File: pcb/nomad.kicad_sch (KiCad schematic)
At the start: 35 parts, among them J1 USB_C_Receptacle_USB2.0_16P, SW1 UP, SW2 DOWN, SW3 RIGHT, SW4 LEFT, SW5 SEL, SW6 SW_Push, SW7 SW_Push, U1 ESP32-S3-WROOM-1, U2 PCF8574T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

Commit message: Updating PCB
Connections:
- net SCL: now also U1.17 (IO9)
- net SDA: now also U1.12 (IO8)
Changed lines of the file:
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@@
+		)
+	)
+	(global_label "FLASHLIGHT"
+		(shape input)
+		(at 195.58 87.63 0)
+		(fields_autoplaced yes)
+		(effects
+			(font
+				(size 1.27 1.27)
+			)
+			(justify left)
+		)
+		(property "Intersheetrefs" "${INTERSHEET_REFS}"
+			(at 209.5115 87.63 0)
+			(hide yes)
+			(show_name no)
+			(do_not_autoplace no)
+			(effects
+				(font
+					(size 1.27 1.27)
+				)
+				(justify left)
+			)
 		)
 	)
@@
 		)
 	)
+	(global_label "SCL"
+		(shape input)
+		(at 236.22 59.69 180)
+		(fields_autoplaced yes)
+		(effects
+			(font
+				(size 1.27 1.27)
+			)
+			(justify right)
+		)
+		(property "Intersheetrefs" "${INTERSHEET_REFS}"
+			(at 229.7272 59.69 0)
+			(hide yes)
+			(show_name no)
+			(do_not_autoplace no)
+			(effects
+				(font
+					(size 1.27 1.27)
+				)
+				(justify right)
+			)
+		)
+	)
 	(global_label "BUTTON_INT"
 		(shape input)
@@
 			)
 		)
+	)
+	(global_label "SDA"
+		(shape input)
+		(at 236.22 57.15 180)
+		(fields_autoplaced yes)
+		(effects
+			(font
+				(size 1.27 1.27)
+			)
+			(justify right)
+		)
+		(property "Intersheetrefs" "${INTERSHEET_REFS}"
+			(at 229.6667 57.15 0)
+			(hide yes)
+			(show_name no)
+			(do_not_autoplace no)
+			(effects
+				(font
+					(size 1.27 1.27)
+				)
+				(justify right)
+			)
+		)

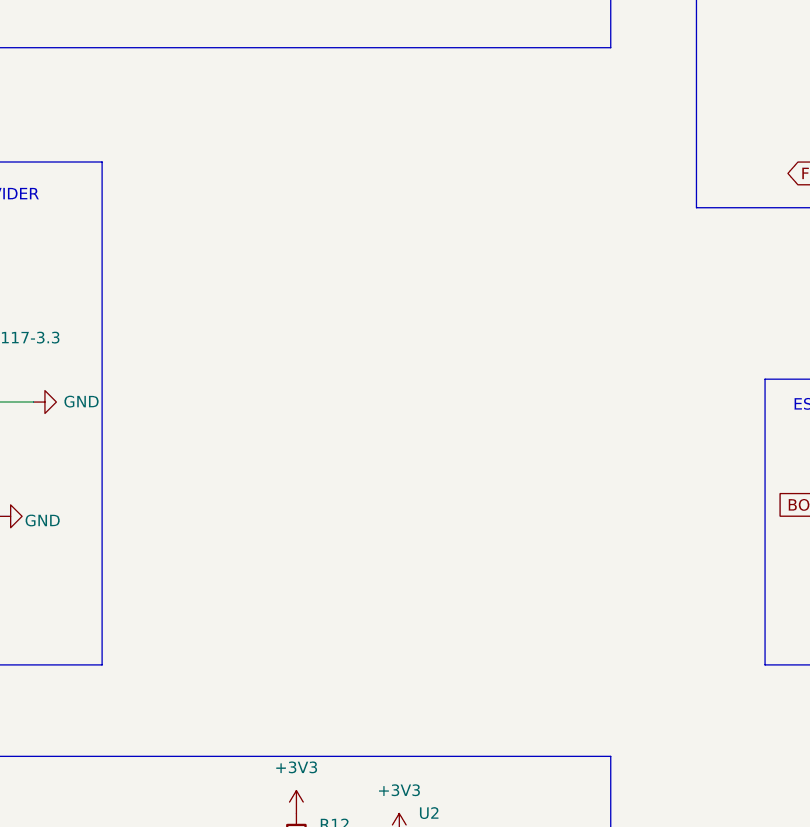
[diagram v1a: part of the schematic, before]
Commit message: Updating footprints & shematics + replacing components on PCB
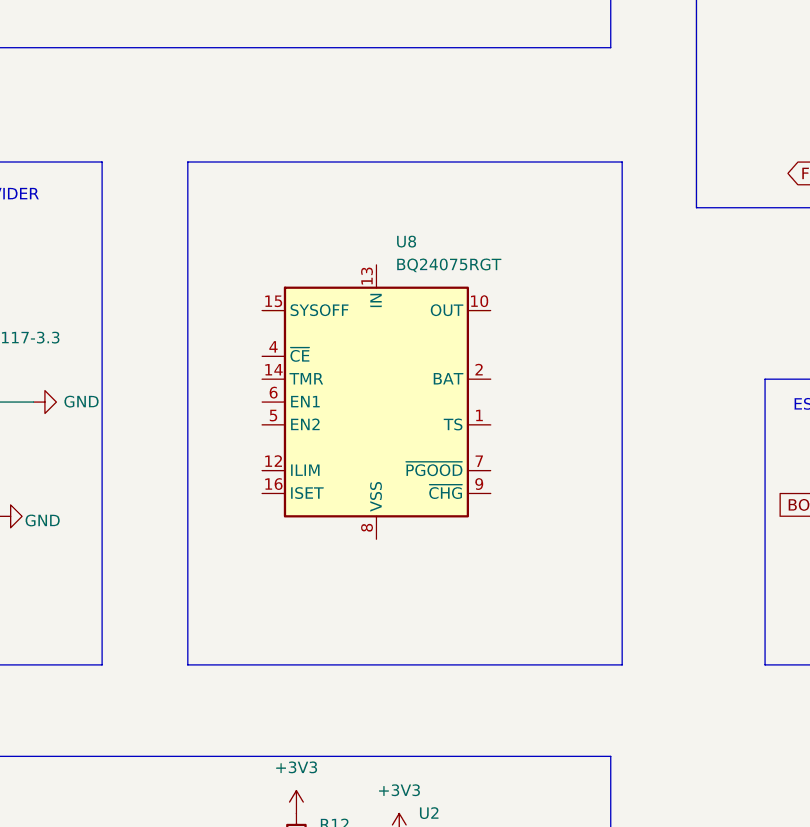
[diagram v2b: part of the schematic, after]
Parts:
- added U8: BQ24075RGT, Package_DFN_QFN:VQFN-16-1EP_3x3mm_P0.5mm_EP1.6x1.6mm, symbol Battery_Management:BQ24075RGT
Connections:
- new net: U8.10 (OUT), U8.11 (OUT)
- new net: U8.17 (VSS), U8.8 (VSS)
- new net: U8.2 (BAT), U8.3 (BAT)
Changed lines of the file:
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@@
 	)
 	(rectangle
+		(start 128.905 86.36)
+		(end 177.165 142.24)
+		(stroke
+			(width 0)
+			(type default)
+		)
+		(fill
+			(type none)
+		)
+	)
+	(rectangle
 		(start 193.04 110.49)
 		(end 260.35 142.24)
@@
 					(unit 1)
 				)
+			)
+		)
+	)
+	(symbol
+		(lib_id "Battery_Management:BQ24075RGT")
+		(at 149.86 113.03 0)
+		(unit 1)
+		(body_style 1)
+		(exclude_from_sim no)
+		(in_bom yes)
+		(on_board yes)
+		(in_pos_files yes)
+		(dnp no)
+		(fields_autoplaced yes)
+		(property "Reference" "U8"
+			(at 152.0033 95.25 0)
+			(show_name no)
+			(do_not_autoplace no)
+			(effects
+				(font
+					(size 1.27 1.27)
+				)
+				(justify left)
+			)
+		)
+		(property "Value" "BQ24075RGT"
+			(at 152.0033 97.79 0)
+			(show_name no)
+			(do_not_autoplace no)
+			(effects
+				(font
+					(size 1.27 1.27)
+				)
+				(justify left)
+			)
+		)
+		(property "Footprint" "Package_DFN_QFN:VQFN-16-1EP_3x3mm_P0.5mm_EP1.6x1.6mm"
+			(at 157.48 127 0)
+			(hide yes)
+			(show_name no)
+			(do_not_autoplace no)
+			(effects
+				(font
+					(size 1.27 1.27)
+				)
+				(justify left)
+			)
+		)
+		(property "Datasheet" "http://www.ti.com/lit/ds/symlink/bq24075.pdf"
+			(at 157.48 107.95 0)
+			(hide yes)
+			(show_name no)
+			(do_not_autoplace no)
+			(effects
+				(font
+					(size 1.27 1.27)
+				)
+			)
+		)
+		(property "Description" "USB-Friendly Li-Ion Battery Charger and Power-Path Management, VQFN-16"
+			(at 149.86 113.03 0)
+			(hide yes)
+			(show_name no)
+			(do_not_autoplace no)
+			(effects
+				(font
+					(size 1.27 1.27)
+				)
+			)
+		)
+		(pin "14"
+		)
+		(pin "15"
+		)
+		(pin "6"
+		)
+		(pin "5"
+		)
+		(pin "1"
+		)
+		(pin "2"
+		)
+		(pin "3"
+		)
+		(pin "9"
+		)
+		(pin "10"
+		)
+		(pin "4"
+		)
+		(pin "8"
+		)
+		(pin "11"
+		)
+		(pin "12"
+		)
+		(pin "16"
+		)
+		(pin "13"
+		)
+		(pin "17"
+		)
+		(pin "7"
+		)
+		(instances
+			(project "nomad"
+				(path "/76473bbd-feb6-4b7c-8160-a4d55fa11a55"
+					(reference "U8")
+					(unit 1)
+				)

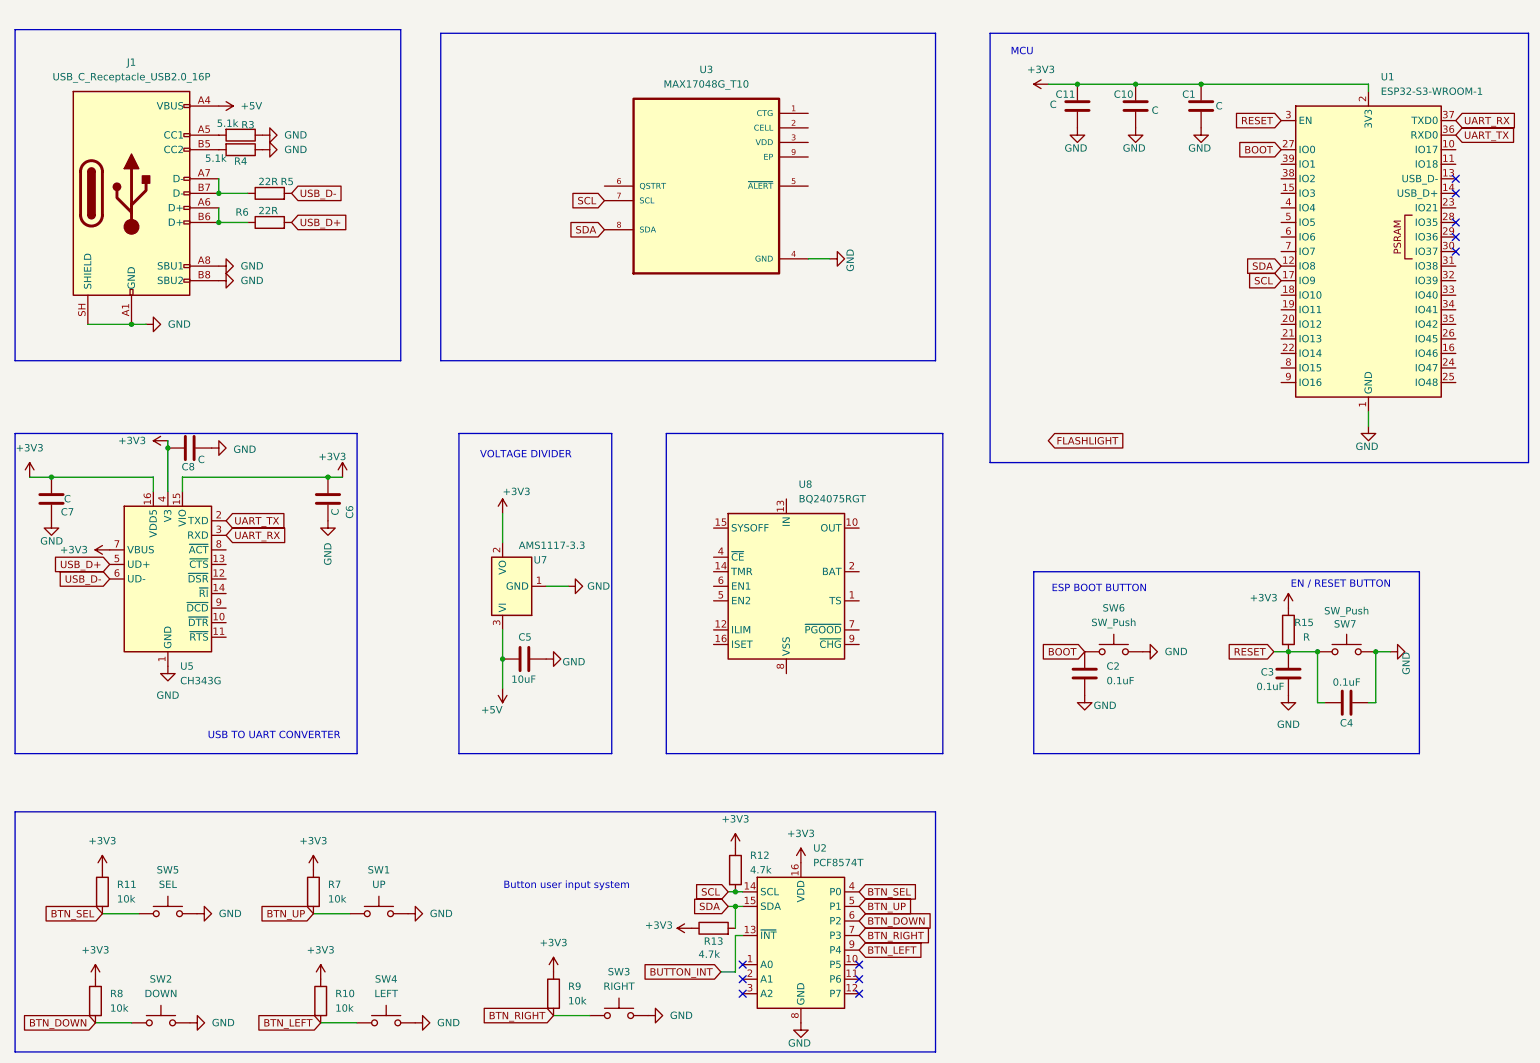
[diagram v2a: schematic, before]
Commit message: Wiring MAX17048 battery percentage module
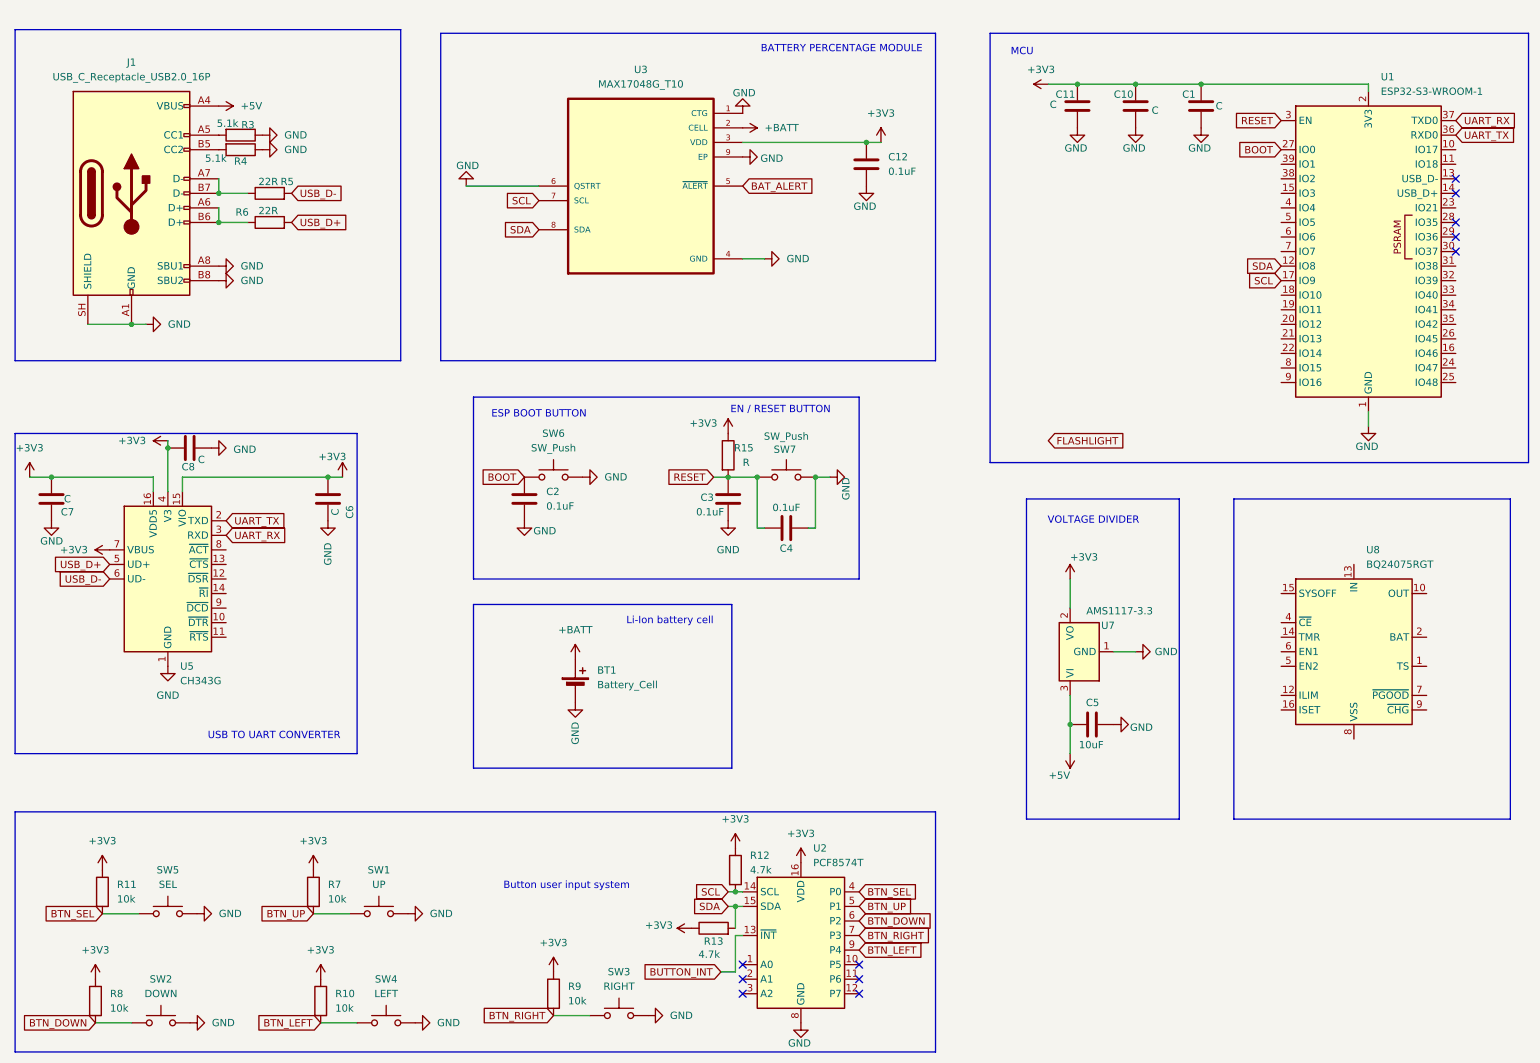
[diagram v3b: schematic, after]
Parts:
- added BT1: Battery_Cell, symbol Device:Battery_Cell
- added C12: 0.1uF, symbol Device:C
- SW1, SW2, SW3, SW4, SW5: footprint Button_Switch_THT:SW_PUSH_6mm -> Button_Switch_SMD:SW_Push_1P1T_NO_E-Switch_TL3301NxxxxxG
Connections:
- net +3V3: now also U3.3 (VDD), C12.1
- net GND: now also U3.1 (CTG), U3.6 (QSTRT), U3.9 (EP), BT1.2 (-), C12.2
- net +BATT: now reaches U3.2 (CELL)
- net +BATT: now also BT1.1 (+)
- net BAT_ALERT: now reaches U3.5 (~{ALERT})
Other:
- note added: "BATTERY PERCENTAGE MODULE"
- note added: "Li-Ion battery cell"
- moved on the sheet: C2, C3, C4, C5, R15, SW6, SW7, U3, U7, U8

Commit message: Updating PCB
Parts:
- removed C6, C7, C8: C, Capacitor_SMD:C_0805_2012Metric, symbol Device:C
- removed U5: CH343G, Package_SO:SOIC-16_3.9x9.9mm_P1.27mm, symbol Interface_USB:CH343G
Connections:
- net USB_D+: now also U1.14 (USB_D+)
- net USB_D-: now also U1.13 (USB_D-)
- net UART_RX: no longer names the net of U1.37 (TXD0)
- no-connect marks 11 -> 10
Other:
- note added: "BATTERY MANAGEMENT"
- note added: "BATTERY SECURITY"
- note added: "USB-C FEMALE PORT FOR CHARGE AND DATA"
- note removed: "USB TO UART CONVERTER"
- moved on the sheet: BT1, C2, C3, C4, R15, SW6, SW7

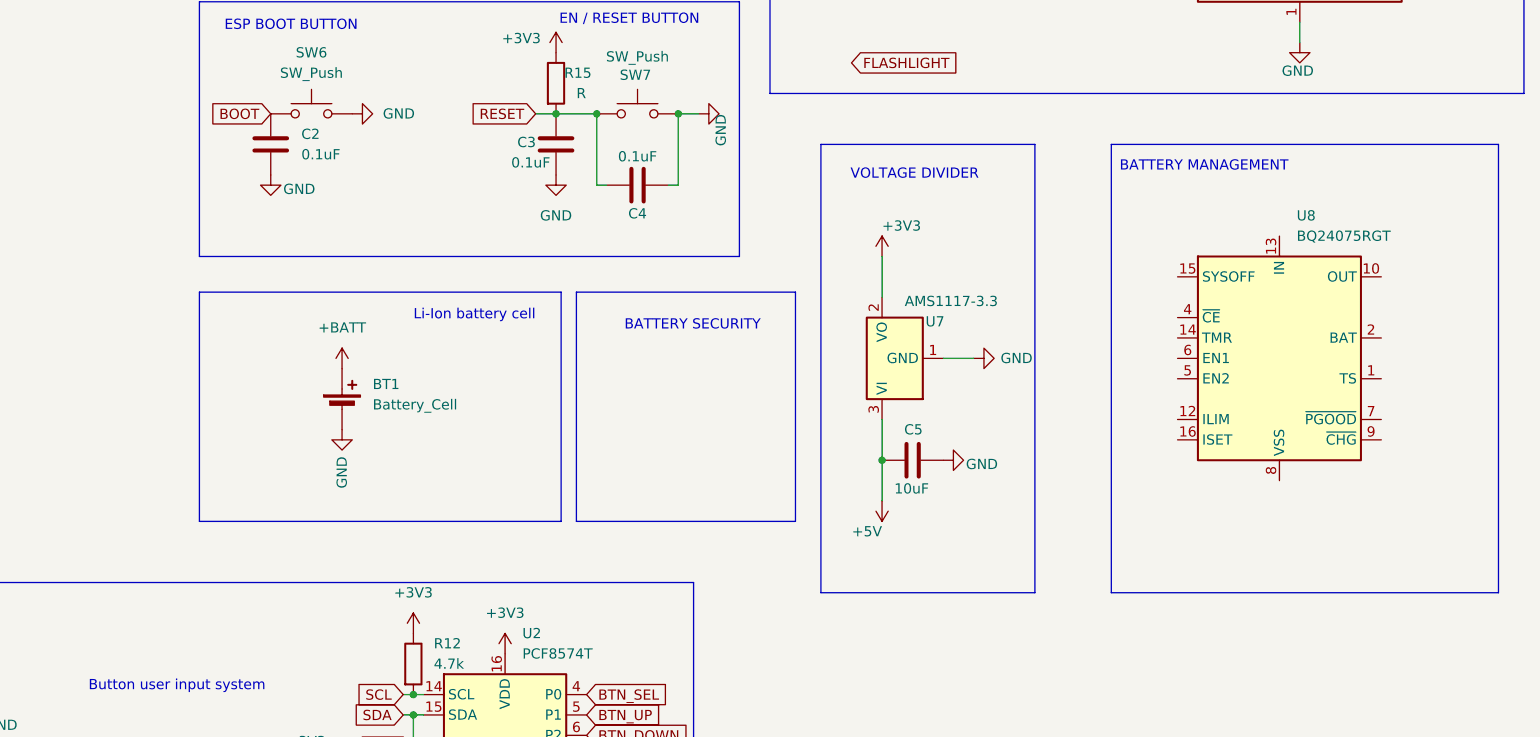
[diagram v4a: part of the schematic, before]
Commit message: Adding battery management system with  MCP73831 chip.
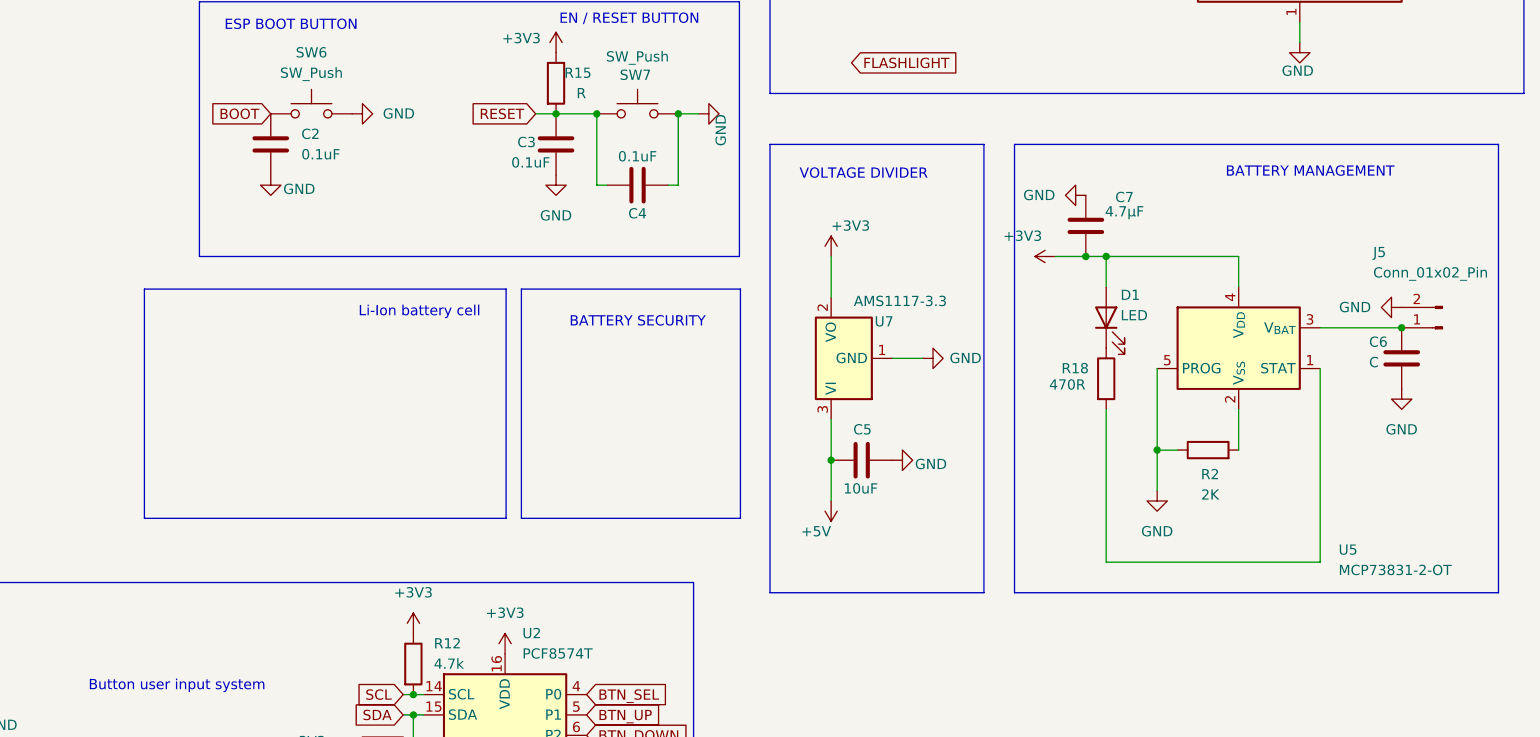
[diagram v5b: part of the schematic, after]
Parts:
- removed BT1: Battery_Cell, symbol Device:Battery_Cell
- removed U8: BQ24075RGT, Package_DFN_QFN:VQFN-16-1EP_3x3mm_P0.5mm_EP1.6x1.6mm, symbol Battery_Management:BQ24075RGT
- added C6: C, Capacitor_SMD:C_0805_2012Metric, symbol Device:C
- added C7: 4.7µF, Capacitor_SMD:C_0805_2012Metric, symbol Device:C
- added D1: LED, symbol Device:LED
- added J5: Conn_01x02_Pin, JST_PH_S2B-PH-K_1x02_P2.00mm_Horizontal, symbol Connector:Conn_01x02_Pin
- added R18: 470R, symbol Device:R
- added R2: 2K, Resistor_SMD:R_0805_2012Metric, symbol Device:R
- added U5: MCP73831-2-OT, Package_TO_SOT_SMD:SOT-23-5, symbol Battery_Management:MCP73831-2-OT
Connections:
- net +3V3: now also C7.1, D1.2 (A), U5.4 (V_{DD})
- net GND: now also C6.2, C7.2, J5.2 (Pin_2), R2.1, U5.5 (PROG)
- new net: C6.1, J5.1 (Pin_1), U5.3 (V_{BAT})
- new net: D1.1 (K), R18.1
- new net: R18.2, U5.1 (STAT)
- new net: R2.2, U5.2 (V_{SS})
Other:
- moved on the sheet: C5, U7
